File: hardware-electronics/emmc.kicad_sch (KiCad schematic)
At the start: 36 parts, among them U2 EMMC16G-MW28-01E10, U4 24AA04T-I_OT, U8 USB2244-AEZG-06, Y2 ECS-240-10-47-CKM-TR

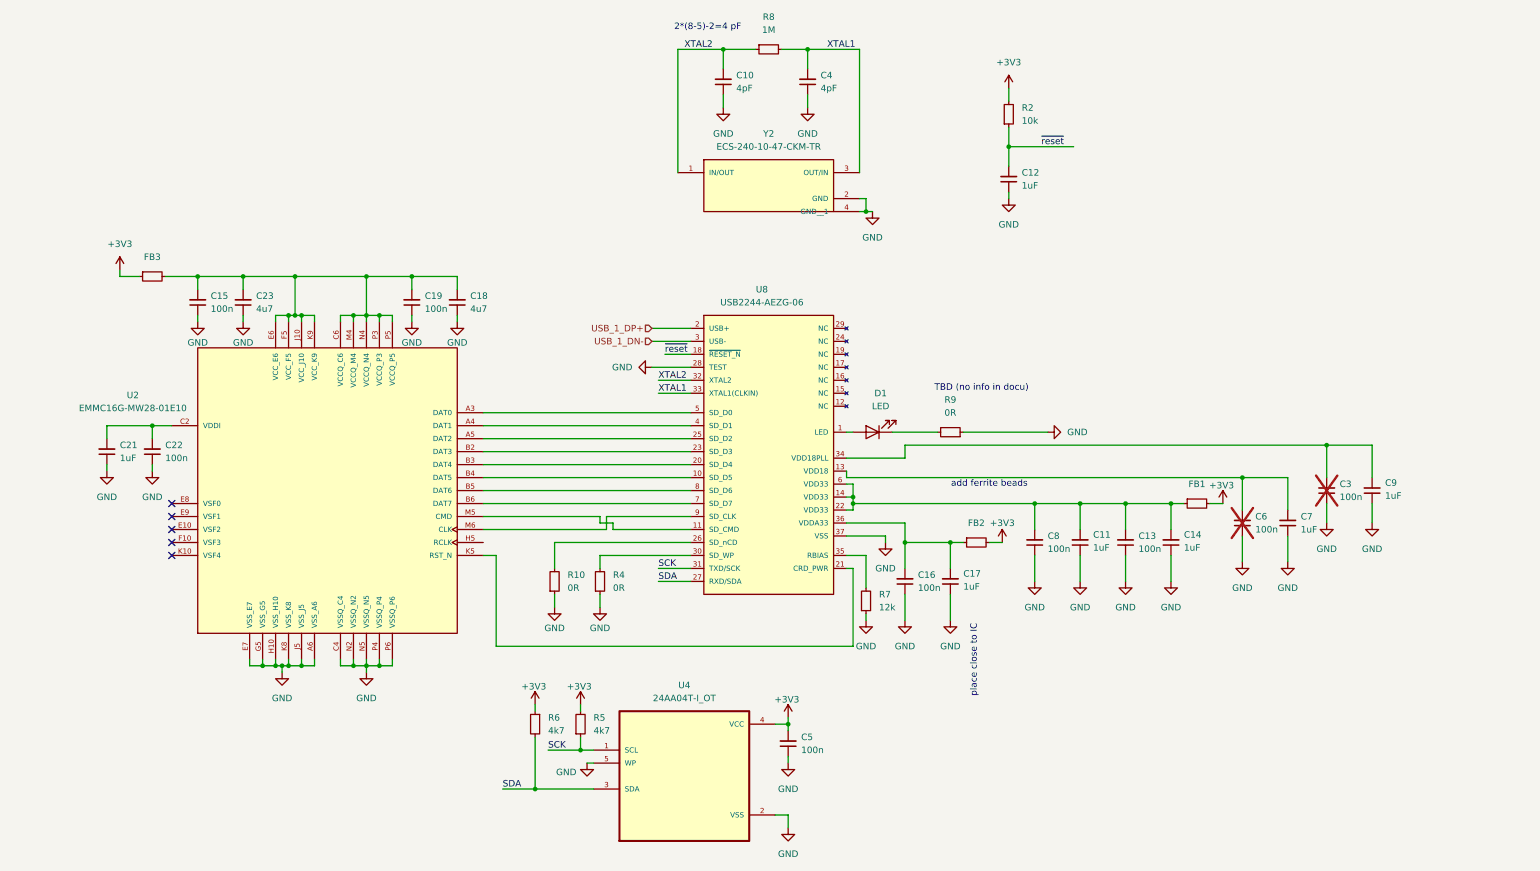
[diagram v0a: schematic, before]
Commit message: #11 SCH EMMC add pull-up capacitors on data lines
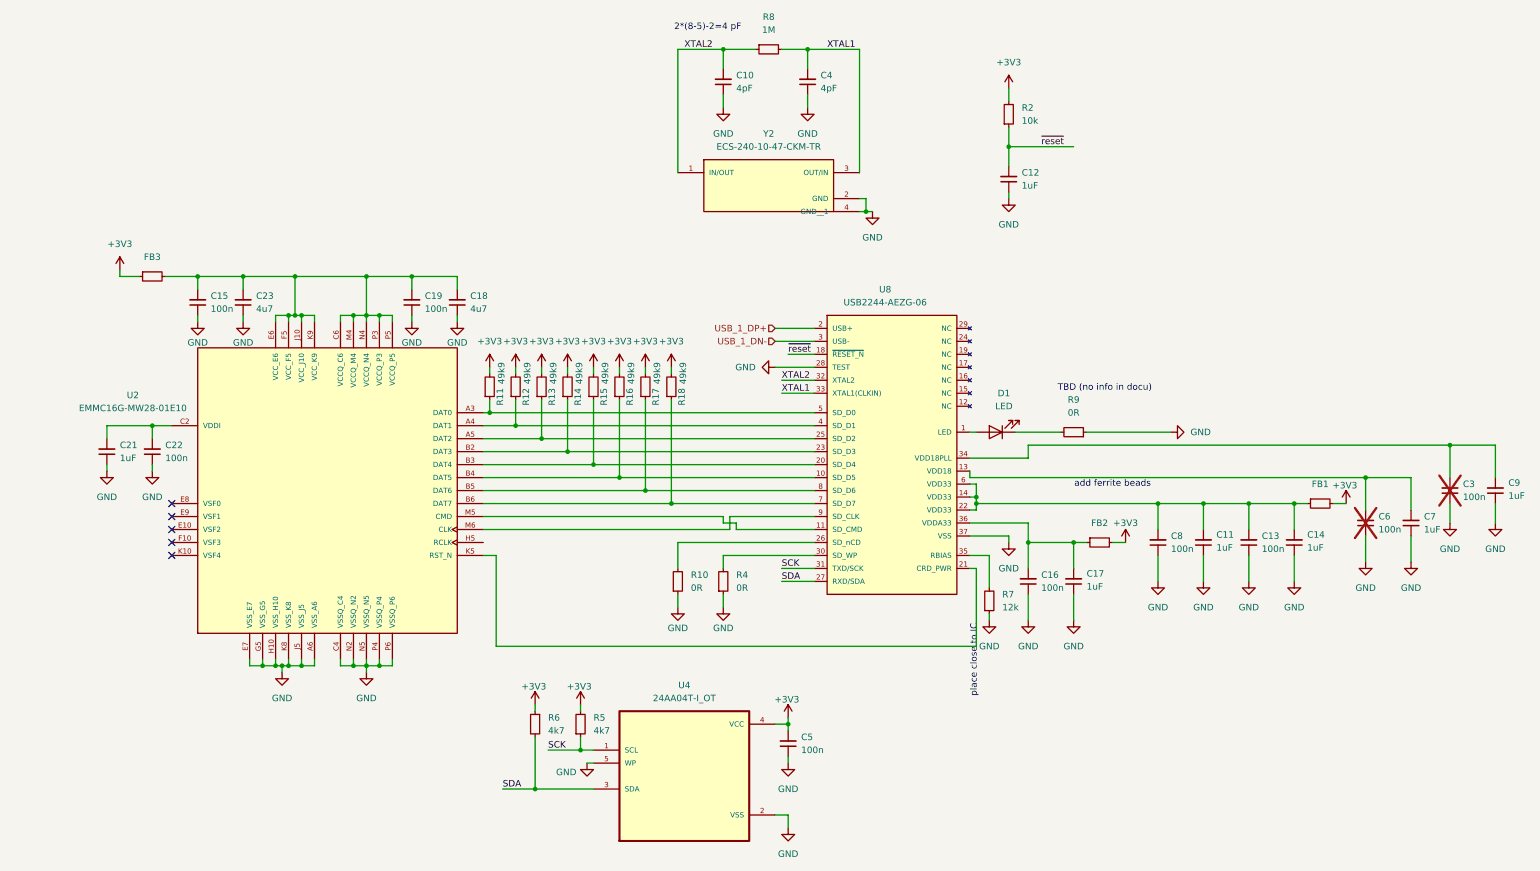
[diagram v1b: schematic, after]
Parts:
- added R11, R12, R13, R14, R15, R16, R17, R18: R_49k9_0402, R_49k9_0402:R_0402_1005Metric, symbol M2SmartHomeSymbols:R_49k9_0402
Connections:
- net +3V3: now also R11.2, R12.2, R13.2, R14.2, R15.2, R16.2, R17.2, R18.2
- net at U2.B4 (DAT5), U8.10 (SD_D5): now also R16.1
- net at U2.B3 (DAT4), U8.20 (SD_D4): now also R15.1
- net at U2.B2 (DAT3), U8.23 (SD_D3): now also R14.1
- net at U2.A5 (DAT2), U8.25 (SD_D2): now also R13.1
- net at U2.A4 (DAT1), U8.4 (SD_D1): now also R12.1
- net at U2.A3 (DAT0), U8.5 (SD_D0): now also R11.1
- net at U2.B6 (DAT7), U8.7 (SD_D7): now also R18.1
- net at U2.B5 (DAT6), U8.8 (SD_D6): now also R17.1
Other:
- moved on the sheet: C11, C13, C14, C16, C17, C3, C6, C7, C8, C9, D1, FB1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

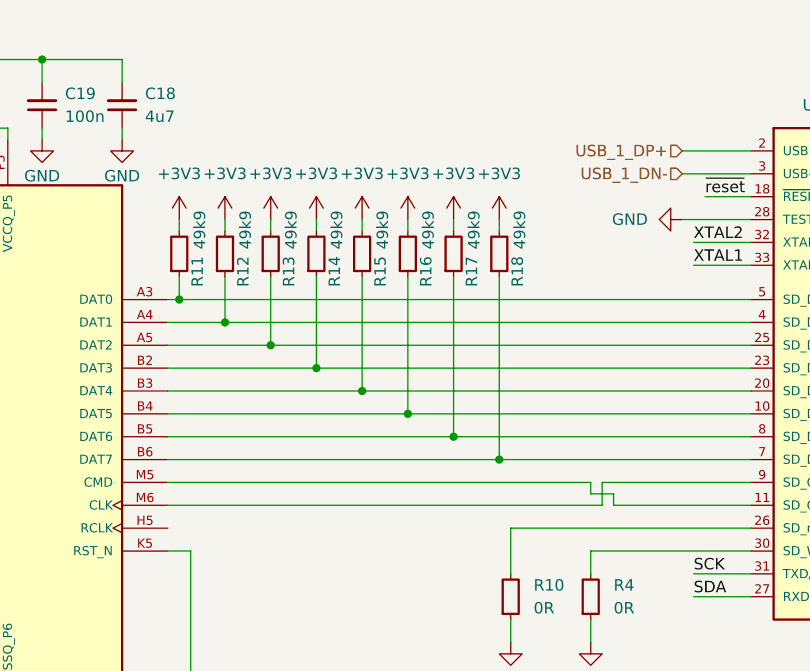
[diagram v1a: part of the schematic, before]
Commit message: #10 SCH SD card copied schematic of USB2244 from emmc
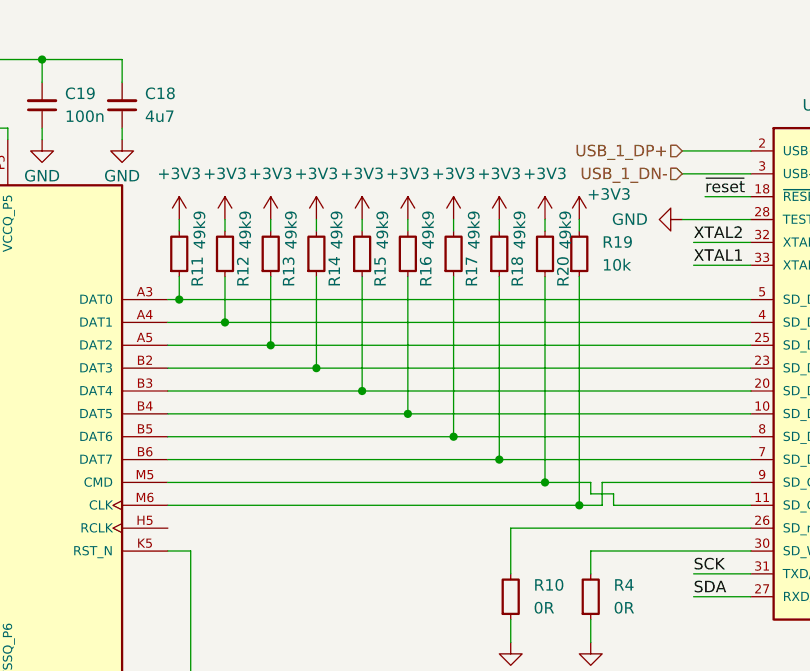
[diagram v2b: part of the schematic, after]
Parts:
- added R19: R_10k_0402, R_10k_0402:R_0402_1005Metric, symbol M2SmartHomeSymbols:R_10k_0402
- added R20: R_49k9_0402, R_49k9_0402:R_0402_1005Metric, symbol M2SmartHomeSymbols:R_49k9_0402
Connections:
- net +3V3: now also R19.2, R20.2
- net at U2.M5 (CMD), U8.11 (SD_CMD): now also R20.1
- net at U2.M6 (CLK), U8.9 (SD_CLK): now also R19.1

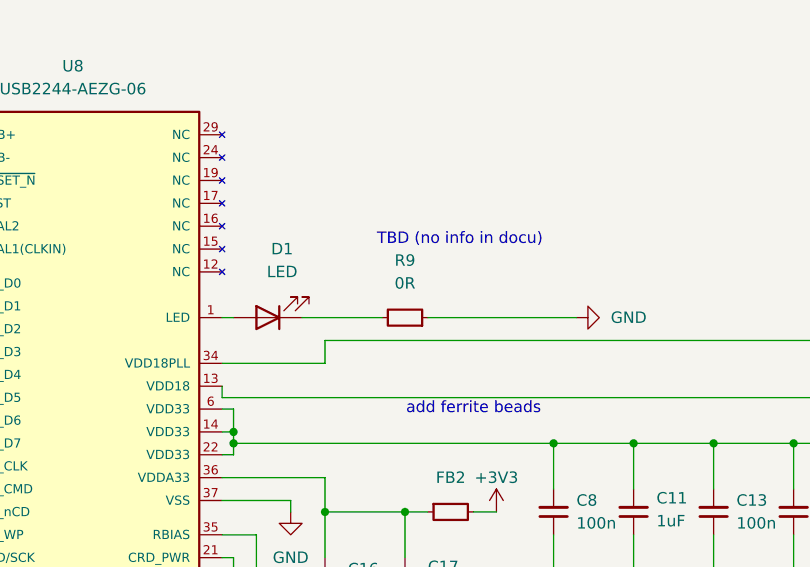
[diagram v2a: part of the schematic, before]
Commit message: #10 SCH SD card connections
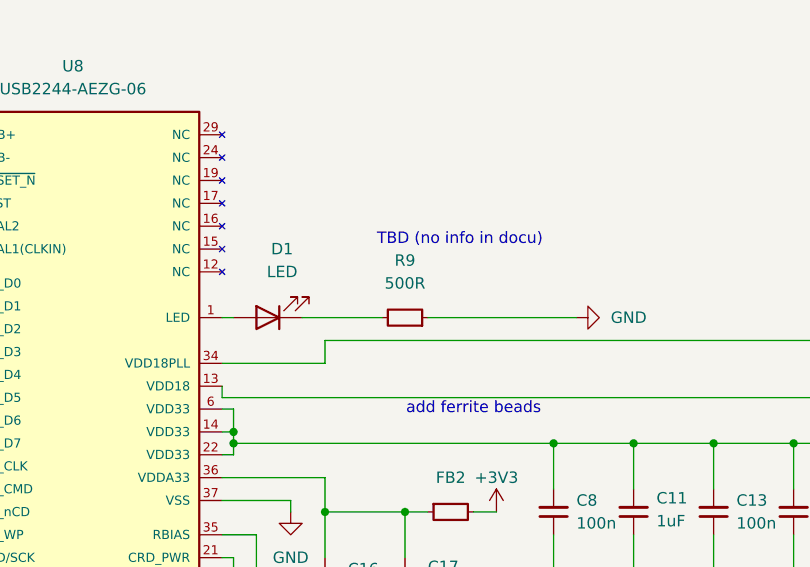
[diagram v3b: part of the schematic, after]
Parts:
- removed R9: R_0_0402, R_0_0402:R_0402_1005Metric, symbol M2SmartHomeSymbols:R_0_0402
- added R9: R_500R_0402, R_500R_0402:R_0402_1005Metric, symbol M2SmartHomeSymbols:R_500R_0402
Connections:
- net GND: now also R9.1
- net at D1.1 (K): now also R9.2
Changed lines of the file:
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@@
+	)
+	(symbol
+		(lib_id "M2SmartHomeSymbols:R_500R_0402")
+		(at 224.79 109.22 180)
+		(unit 1)
+		(exclude_from_sim no)
+		(in_bom yes)
+		(on_board yes)
+		(dnp no)
+		(fields_autoplaced yes)
+		(property "Reference" "R9"
+			(at 222.25 102.87 0)
+			(effects
+				(font
+					(size 1.27 1.27)
+					(thickness 0.15)
+				)
+			)
+		)
+		(property "Value" "R_500R_0402"
+			(at 204.47 96.52 0)
+			(effects
+				(font
+					(size 1.27 1.27)
+					(thickness 0.15)
+				)
+				(justify left bottom)
+				(hide yes)
+			)
+		)
+		(property "Footprint" "R_500R_0402:R_0402_1005Metric"
+			(at 204.47 93.98 0)
+			(effects
+				(font
+					(size 1.27 1.27)
+					(thickness 0.15)
+				)
+				(justify left bottom)
+				(hide yes)
+			)
+		)
+		(property "Datasheet" "https://www.vishay.com/docs/20035/crcw0402.pdf"
+			(at 204.47 91.44 0)
+			(effects
+				(font
+					(size 1.27 1.27)
+					(thickness 0.15)
+				)
+				(justify left bottom)
+				(hide yes)
+			)
+		)
+		(property "Description" "SMD Thick Film Resistor, 500 Ω, ±1%, 1/16 W, 0402 [1005 Metric], CRCW Series"
+			(at 224.79 109.22 0)
+			(effects
+				(font
+					(size 1.27 1.27)
+				)
+				(hide yes)
+			)
+		)
+		(property "MPN" "CRCW0402500RFKED"
+			(at 204.47 88.9 0)
+			(effects
+				(font
+					(size 1.27 1.27)
+					(thickness 0.15)
+				)
+				(justify left bottom)
+				(hide yes)
+			)
+		)
+		(property "Manufacturer" "Vishay"
+			(at 204.47 86.36 0)
+			(effects
+				(font
+					(size 1.27 1.27)
+					(thickness 0.15)
+				)
+				(justify left bottom)
+				(hide yes)
+			)
+		)
+		(property "License" "Apache-2.0"
+			(at 204.47 83.82 0)
+			(effects
+				(font
+					(size 1.27 1.27)
+					(thickness 0.15)
+				)
+				(justify left bottom)
+				(hide yes)
+			)
+		)
+		(property "Author" "Your Name"
+			(at 204.47 81.28 0)
+			(effects
+				(font
+					(size 1.27 1.27)
+					(thickness 0.15)
+				)
+				(justify left bottom)
+				(hide yes)
+			)
+		)
+		(property "Val" "500R"
+			(at 222.25 105.41 0)
+			(effects
+				(font
+					(size 1.27 1.27)
+					(thickness 0.15)
+				)
+			)
+		)
+		(property "Tolerance" "1%"
+			(at 204.47 99.06 0)
+			(effects
+				(font
+					(size 1.27 1.27)
+				)
+				(justify left bottom)
+				(hide yes)
+			)
+		)
+		(property "Power" "1/16 W"
+			(at 204.47 95.52 0)
+			(effects
+				(font
+					(size 1.27 1.27)
+				)
+				(justify left bottom)
+				(hide yes)
+			)
+		)
+		(pin "2"
+		)
+		(pin "1"
+		)
+		(instances
+			(project "M2SmartHome"
+				(path "/da663dec-9e91-4003-a791-431d460ad63c/d6ad415e-1295-4f8b-8193-bff1569600a2"
+					(reference "R9")
+					(unit 1)
+				)
+			)
+		)
 	)
 	(symbol
@@
 					(unit 1)
 				)
-			)
-		)
-	)
-	(symbol
-		(lib_id "M2SmartHomeSymbols:R_0_0402")
-		(at 224.79 109.22 180)
-		(unit 1)
-		(exclude_from_sim no)
-		(in_bom yes)
-		(on_board yes)
-		(dnp no)
-		(fields_autoplaced yes)
-		(property "Reference" "R9"
-			(at 222.25 102.87 0)
-			(effects
-				(font
-					(size 1.27 1.27)
-					(thickness 0.15)
-				)
-			)
-		)
-		(property "Value" "R_0_0402"
-			(at 204.47 96.52 0)
-			(effects
-				(font
-					(size 1.27 1.27)
-					(thickness 0.15)
-				)
-				(justify left bottom)
-				(hide yes)
-			)
-		)
-		(property "Footprint" "R_0_0402:R_0402_1005Metric"
-			(at 204.47 93.98 0)
-			(effects
-				(font
-					(size 1.27 1.27)
-					(thickness 0.15)
-				)
-				(justify left bottom)
-				(hide yes)
-			)
-		)
-		(property "Datasheet" "https://www.vishay.com/docs/20035/crcw0402.pdf"
-			(at 204.47 91.44 0)
-			(effects
-				(font
-					(size 1.27 1.27)
-					(thickness 0.15)
-				)
-				(justify left bottom)
-				(hide yes)
-			)
-		)
-		(property "Description" "SMD Thick Film Resistor, 0 Ω, Jumper, 1/16 W, 0402 [1005 Metric], CRCW Series"
-			(at 224.79 109.22 0)
-			(effects
-				(font
-					(size 1.27 1.27)
-				)
-				(hide yes)
-			)
-		)
-		(property "MPN" "CRCW04020000Z0ED"
-			(at 204.47 88.9 0)
-			(effects
-				(font
-					(size 1.27 1.27)
-					(thickness 0.15)
-				)
-				(justify left bottom)
-				(hide yes)
-			)
-		)
-		(property "Manufacturer" "Vishay"
-			(at 204.47 86.36 0)
-			(effects
-				(font
-					(size 1.27 1.27)
-					(thickness 0.15)
-				)
-				(justify left bottom)
-				(hide yes)
-			)
-		)
-		(property "License" "Apache-2.0"
-			(at 204.47 83.82 0)
-			(effects
-				(font
-					(size 1.27 1.27)
-					(thickness 0.15)
-				)
-				(justify left bottom)
-				(hide yes)
-			)
-		)
-		(property "Author" "Your Name"
-			(at 204.47 81.28 0)
-			(effects
-				(font
-					(size 1.27 1.27)
-					(thickness 0.15)
-				)
-				(justify left bottom)
-				(hide yes)
-			)
-		)
-		(property "Val" "0R"
-			(at 222.25 105.41 0)
-			(effects
-				(font
-					(size 1.27 1.27)
-					(thickness 0.15)
-				)
-			)
-		)
-		(property "Power" "1/16 W"
-			(at 204.47 99.06 0)
-			(effects
-				(font
-					(size 1.27 1.27)
-				)
-				(justify left bottom)
-				(hide yes)
-			)
-		)
-		(pin "1"
-		)
-		(pin "2"
-		)
-		(instances
-			(project "M2SmartHome"
-				(path "/da663dec-9e91-4003-a791-431d460ad63c/d6ad415e-1295-4f8b-8193-bff1569600a2"
-					(reference "R9")
-					(unit 1)
-				)

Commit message: SCH cosmetic changes
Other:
- note removed: "add ferrite beads"
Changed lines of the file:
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@@
-		)
-	)
-	(text "add ferrite beads"
-		(exclude_from_sim no)
-		(at 229.87 119.38 0)
-		(effects
-			(font
-				(size 1.27 1.27)
-			)
 		)
 	)

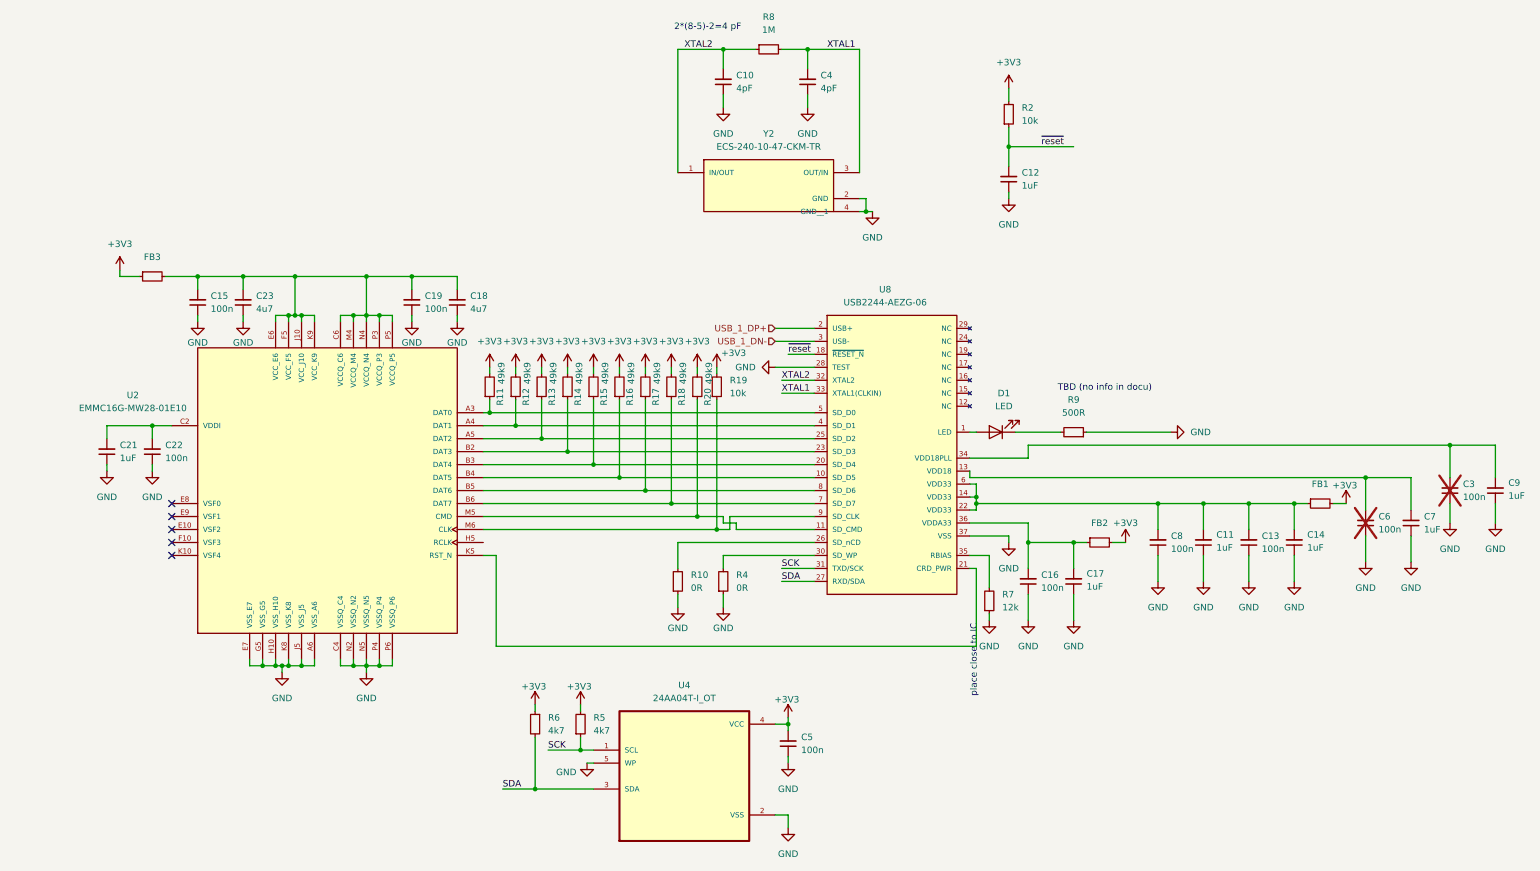
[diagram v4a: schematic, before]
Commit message: [#11] SCH eMMC replaced power symbols
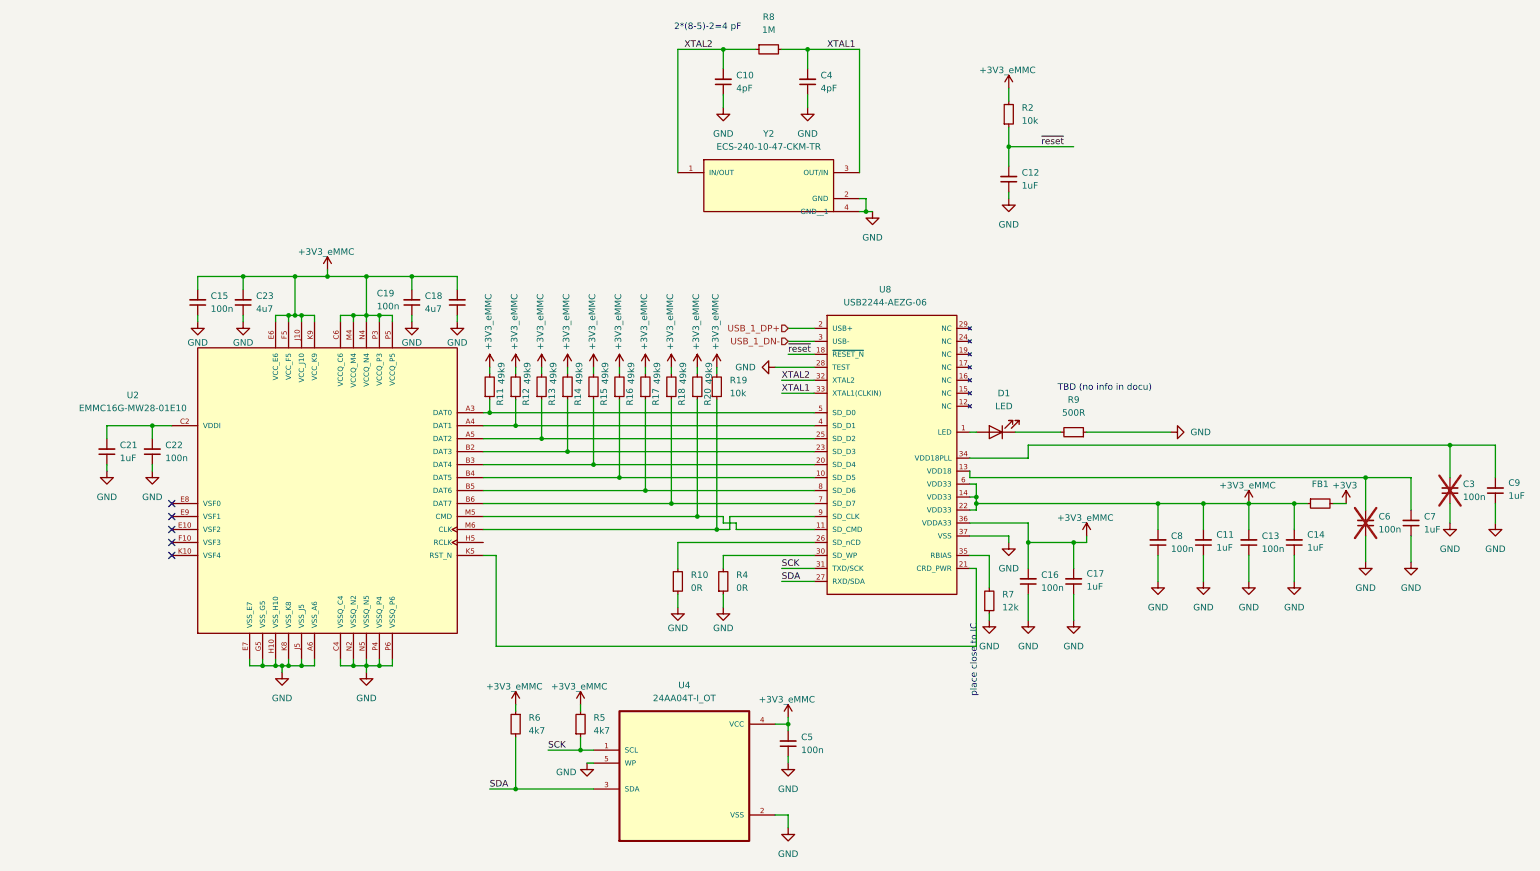
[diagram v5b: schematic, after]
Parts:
- removed FB2, FB3: FB_120R_0603, FB_120R_0603:FB_0603_1608Metric, symbol M2SmartHomeSymbols:FB_120R_0603
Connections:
- net +3V3: no longer C5.2, R11.2, R12.2, R13.2, R14.2, R15.2, R16.2, R17.2, R18.2, R19.2, R2.2, R20.2, R5.2, R6.1, U4.4 (VCC)
- net +3V3_eMMC: now reaches C11.2, C13.2, C14.2, C8.2, FB1.1, U8.14 (VDD33), U8.22 (VDD33), U8.6 (VDD33)
- net +3V3_eMMC: now also C15.2, C16.2, C17.2, C18.2, C19.2, C23.2, C5.2, R11.2, R12.2, R13.2, R14.2, R15.2, R16.2, R17.2, R18.2, R19.2, R2.2, R20.2, R5.2, R6.1, U2.C6 (VCCQ_C6), U2.E6 (VCC_E6), U2.F5 (VCC_F5), U2.J10 (VCC_J10), U2.K9 (VCC_K9), U2.M4 (VCCQ_M4), U2.N4 (VCCQ_N4), U2.P3 (VCCQ_P3), U2.P5 (VCCQ_P5), U4.4 (VCC), U8.36 (VDDA33)
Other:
- moved on the sheet: R6

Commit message: SCH cosmetic changes
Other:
- moved on the sheet: C10, C11, C12, C13, C14, C15, C16, C17, C18, C19, C21, C22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
